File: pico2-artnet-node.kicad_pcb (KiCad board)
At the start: 2 copper layers, 84.6 x 157.4 mm, 116 parts, among them J1 USB_C_Receptacle_PowerOnly_6P, J2 NC3FAAH, J3 NC3FAAH, J4 NC3FAAH, J5 NC3FAAH, J6 Conn_01x02_Pin, J7 I2C Header, J8 Conn_01x16_Pin, U1 WIZPoE Hat, U2 W5500-EVB-PICO2, U3 AMS1117-3.3, U4 B0505S-2WR3, U5 ISO1410BDWR, U6 ISO1410BDWR, U7 ISO1410BDWR, U8 ISO1410BDWR, U9 SN74LVC4245APWR

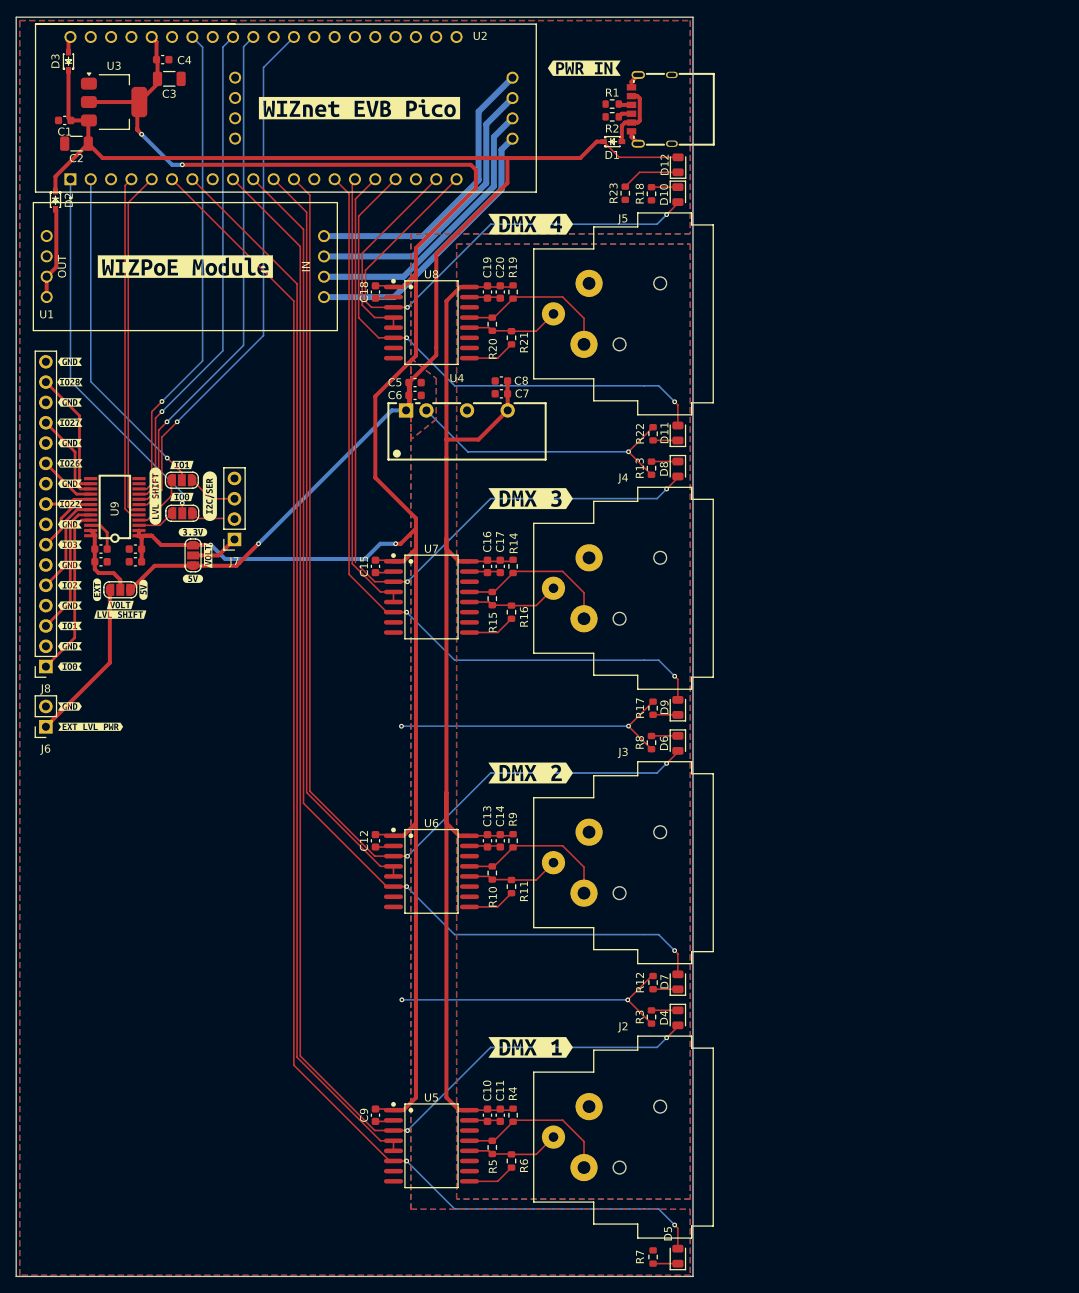
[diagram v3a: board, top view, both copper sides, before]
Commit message: change solder jumpers to pins & power break out
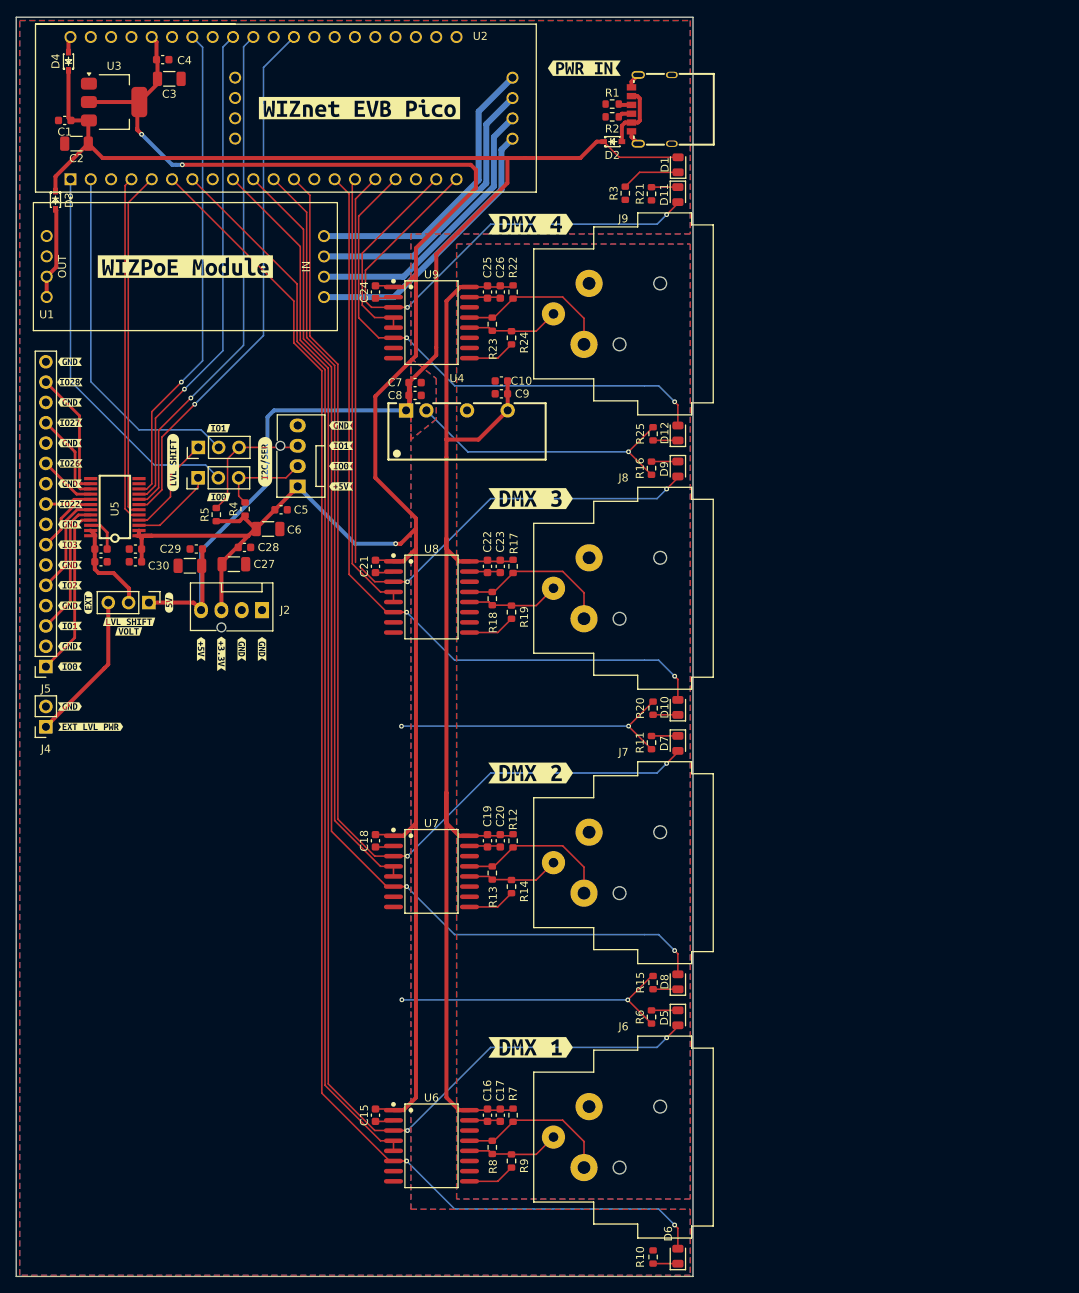
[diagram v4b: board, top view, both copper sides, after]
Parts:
- removed JP4: I2C Volt Sel, Jumper:SolderJumper-3_P1.3mm_Open_RoundedPad1.0x1.5mm
- removed kibuzzard-68DD1EE6: G***, kibuzzard-68DD1EE6
- removed the kibuzzard-68DD1F80 at (67.4, 105.0)
- removed kibuzzard-68DD1F8F: G***, kibuzzard-68DD1F8F
- added C27: 100u, Capacitor_SMD:C_1206_3216Metric, F.Cu at (72.5, 103.2)
- added C28: 10u, Capacitor_SMD:C_0603_1608Metric, F.Cu at (73.8, 101.1)
- added C29: 10u, Capacitor_SMD:C_0603_1608Metric, F.Cu at (67.8, 101.3)
- added C30: 100u, Capacitor_SMD:C_1206_3216Metric, F.Cu at (67.0, 103.4)
- added C5: 10u, Capacitor_SMD:C_0603_1608Metric, F.Cu at (78.4, 96.4)
- added C6: 100u, Capacitor_SMD:C_1206_3216Metric, F.Cu at (76.8, 98.8)
- added J2: Conn_01x04_Pin, Connector:FanPinHeader_1x04_P2.54mm_Vertical, F.Cu at (76.0, 108.9)
- added R4: 4.7k, Resistor_SMD:R_0603_1608Metric, F.Cu at (73.9, 96.3)
- added R5: 4.7k, Resistor_SMD:R_0603_1608Metric, F.Cu at (70.3, 97.0)
- added kibuzzard-68DD43ED: G***, kibuzzard-68DD43ED, F.Cu at (76.0, 113.8)
- added kibuzzard-68DD43ED: G***, kibuzzard-68DD43ED, F.Cu at (85.9, 85.9)
- added kibuzzard-68DD4448: G***, kibuzzard-68DD4448, F.Cu at (85.9, 88.4)
- added kibuzzard-68DD444E: G***, kibuzzard-68DD444E, F.Cu at (85.9, 90.9)
- added kibuzzard-68DD4454: G***, kibuzzard-68DD4454, F.Cu at (85.9, 93.5)
- added kibuzzard-68DD4454: G***, kibuzzard-68DD4454, F.Cu at (68.4, 113.8)
- added kibuzzard-68DD5009: G***, kibuzzard-68DD5009, F.Cu at (70.9, 114.4)
- added kibuzzard-68DD501A: G***, kibuzzard-68DD501A, F.Cu at (73.5, 113.8)
- J3: renamed from J7; footprint Connector_PinSocket_2.54mm:PinSocket_1x04_P2.54mm_Vertical -> Connector:FanPinHeader_1x04_P2.54mm_Vertical
- JP1, JP2, JP3: footprint Jumper:SolderJumper-3_P1.3mm_Open_RoundedPad1.0x1.5mm -> Connector_PinHeader_2.54mm:PinHeader_1x03_P2.54mm_Vertical
- moved J3 10.3 mm to (80.5, 93.5), turned to 90 degrees
- moved kibuzzard-68DD1F08 8.13 mm to (76.4, 90.4)
- moved kibuzzard-68DD1E9C 6.48 mm to (70.6, 86.2)
- moved JP2 4.85 mm to (68.0, 92.4), turned to 90 degrees
- moved kibuzzard-68DD1EFE 4.74 mm to (64.9, 90.5)
- moved kibuzzard-68DD1E8E 4.60 mm to (70.6, 94.8)
- moved JP3 4.59 mm to (68.1, 88.6), turned to 90 degrees
- moved JP1 3.92 mm to (61.9, 108.0), turned to -90 degrees
- moved kibuzzard-68DD1F80 3.58 mm to (64.4, 108.0)
- moved kibuzzard-68DD23A7 3.46 mm to (59.3, 111.6)
- moved kibuzzard-68DD2361 1.94 mm to (54.3, 108.0)
- moved kibuzzard-68DD23B6 1.42 mm to (59.4, 110.4)
- renumbered C8 to C10, C23 to C11, C24 to C12, C21 to C13, C22 to C14, C9 to C15, C10 to C16, C11 to C17, C12 to C18, C13 to C19, C14 to C20, C15 to C21, C16 to C22, C17 to C23, C18 to C24, C19 to C25, C20 to C26, C5 to C7, C6 to C8, C7 to C9, D12 to D1, D9 to D10, D10 to D11, D11 to D12, D1 to D2, D2 to D3, D3 to D4, D4 to D5, D5 to D6, D6 to D7, D7 to D8, D8 to D9, J6 to J4, J8 to J5, J2 to J6, J3 to J7, J4 to J8, J5 to J9, R7 to R10, R8 to R11, R9 to R12, R10 to R13, R11 to R14, R12 to R15, R13 to R16, R14 to R17, R15 to R18, R16 to R19, R17 to R20, R18 to R21, R19 to R22, R20 to R23, R21 to R24, R22 to R25, R23 to R3, R3 to R6, R4 to R7, R5 to R8, R6 to R9, U9 to U5, U5 to U6, U6 to U7, U7 to U8, U8 to U9
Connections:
- J3 pad 1: Net-(J7-Pin_1) -> +3V3
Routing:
- net +3V3: track 252.7 -> 272.9 mm, vias 4 -> 3
- net +5V: track 175.9 -> 192.0 mm, vias 1 -> 0
- net Net-(J3-Pin_3): track 6.24 -> 16.2 mm
- net Net-(J3-Pin_2): track 4.07 -> 11.4 mm
- net Net-(J7-Pin_1): track 6.00 -> 0.00 mm
- net LVL SHIFT A1: track 4.73 -> 10.5 mm
- net LVL SHIFT A2: track 7.47 -> 12.8 mm
- net Net-(JP1-C): track 10.0 -> 12.1 mm
- net GPIO1: track 42.6 -> 44.7 mm, vias 1 -> 0
- net Net-(J4-Pin_1): track 20.4 -> 18.8 mm
- net GPIO0: track 47.5 -> 48.7 mm, vias 1 -> 0

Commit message: remove PoE Breakout & rund DRC
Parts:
- removed D3, D4: B0520WS, EasyEDA:SOD-323_L1.7-W1.3-LS2.6-RD-1
- removed U1: WIZPoE Hat, W5500-EVB-PICO:WIZPoE Hat
- removed U3: AMS1117-3.3, Package_TO_SOT_SMD:SOT-223-3_TabPin2
- removed kibuzzard-68DD286D: G***, kibuzzard-68DD286D
- J1: footprint EasyEDA:USB-C-SMD_YPE-C-6PWTL-10-0108 -> EasyEDA:USB-C-SMD_YPE-C-6PWTL-10-0108_Board-overhang
- J6, J7, J8, J9: footprint Connector_Audio:Jack_XLR_Neutrik_NC3FAAH_Horizontal -> Connector_Audio:Jack_XLR_Neutrik_NC3FAAH_Horizontal_Board-Overhang
- moved C2 69.1 mm to (121.9, 52.6), turned to 0 degrees
- moved C1 69.0 mm to (120.3, 50.4), turned to 0 degrees
- moved R4 9.60 mm to (73.8, 86.7)
- moved C11 9.18 mm to (55.9, 92.1)
- moved C12 9.18 mm to (55.9, 93.7)
- moved C13 9.18 mm to (60.2, 93.7)
- moved C14 9.18 mm to (60.2, 92.1)
- moved C27 9.18 mm to (72.5, 94.0)
- moved C30 9.18 mm to (67.0, 94.2)
- moved C5 9.18 mm to (78.4, 87.2)
- moved J3 9.18 mm to (80.5, 84.3)
- moved J4 9.18 mm to (49.0, 114.3)
- moved JP2 9.18 mm to (68.0, 83.2)
- moved kibuzzard-68DD1E9C 9.18 mm to (70.5, 77.0)
- moved kibuzzard-68DD1F08 9.18 mm to (76.4, 81.2)
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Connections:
- C1 pad 1: +5V -> +5V USB
- C2 pad 1: +5V -> +5V USB
- U2 pad 37: GND -> unconnected-(U2-3V3_EN-Pad37)
- U2 pad 39: unconnected-(U2-VSYS-Pad39) -> +5V
- U2 pad 40: +5V RP -> unconnected-(U2-VBUS-Pad40)
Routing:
- net Net-(U1-VC2-): track 36.8 -> 0.00 mm
- net Net-(U1-VC2+): track 36.1 -> 0.00 mm
- net Net-(U1-VC1-): track 35.4 -> 0.00 mm
- net Net-(U1-VC1+): track 34.7 -> 0.00 mm
- net +5V: track 192.0 -> 166.8 mm, vias 0 -> 1
- net +3V3: track 272.9 -> 253.0 mm, vias 3 -> 1
- net +5V PoE: track 11.5 -> 0.00 mm
- net GPIO1: track 44.7 -> 35.5 mm
- net GPIO0: track 48.7 -> 39.5 mm
- net GPIO2: track 43.6 -> 34.4 mm
- net GPIO3: track 43.7 -> 34.5 mm
- net GPIO22: track 67.1 -> 57.9 mm
- net GPIO26: track 64.3 -> 55.1 mm
- net GPIO27: track 62.6 -> 53.4 mm
- net GPIO28: track 60.9 -> 53.5 mm
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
